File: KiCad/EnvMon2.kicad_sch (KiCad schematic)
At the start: 35 parts, among them J1 USB-C, J2 DC, J3 TEMP, M1 OLED1.5-RGB, SW1 SW_Push, SW2 SW_Push, SW3 SW_Push, U1 LMR16006+FB, U2 SCD41, U3 FT231XQ, U4 ESP32-PICO-MINI-02, U5 QR

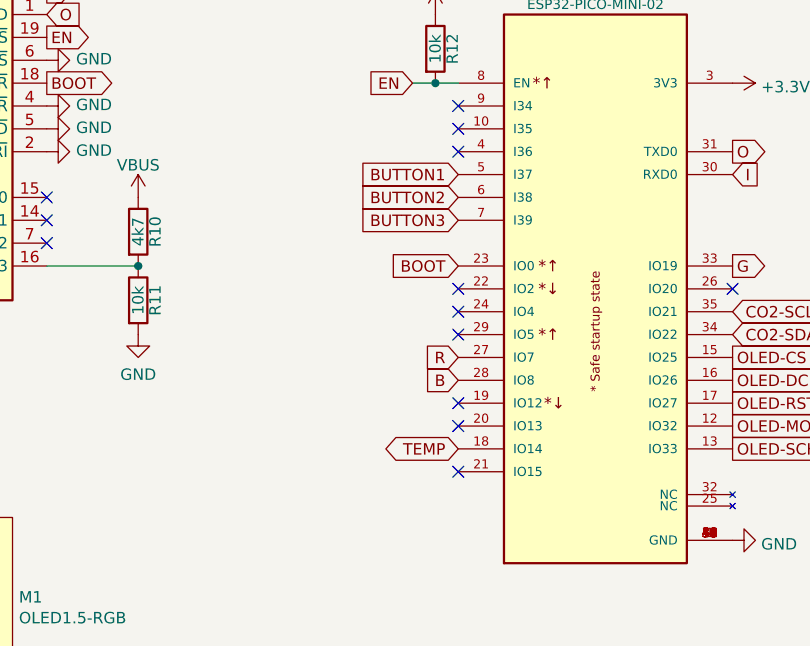
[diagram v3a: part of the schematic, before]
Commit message: Tidy GPIO usage for buttons
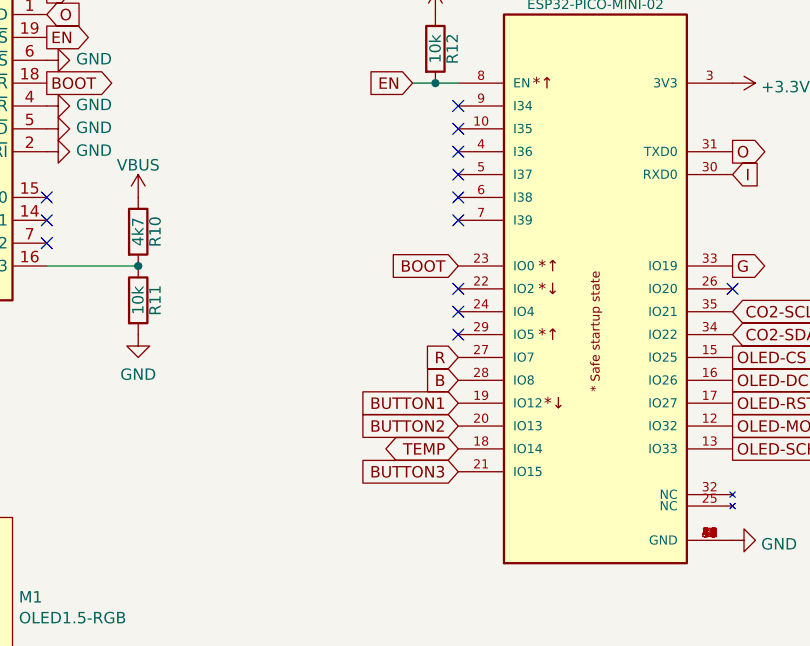
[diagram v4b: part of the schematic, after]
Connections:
- net BUTTON1: now also U4.19 (IO12); no longer U4.5 (I37)
- net BUTTON2: now also U4.20 (IO13); no longer U4.6 (I38)
- net BUTTON3: now also U4.21 (IO15); no longer U4.7 (I39)
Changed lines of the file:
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@@
   (no_connect (at 149.86 50.8))
   (no_connect (at 149.86 53.34))
-  (no_connect (at 195.58 76.2))
-  (no_connect (at 195.58 81.28))
+  (no_connect (at 195.58 50.8))
+  (no_connect (at 195.58 53.34))
   (no_connect (at 226.06 60.96))
   (no_connect (at 195.58 40.64))
@@
   (no_connect (at 195.58 60.96))
   (no_connect (at 195.58 66.04))
-  (no_connect (at 195.58 73.66))
+  (no_connect (at 195.58 48.26))
   (no_connect (at 195.58 63.5))
   (wire (pts (xy 55.88 33.02) (xy 58.42 33.02))
@@
     )
   )
-  (global_label "BUTTON2" (shape input) (at 195.58 50.8 180) (fields_autoplaced)
-    (effects (font (size 1.27 1.27)) (justify right))
-    (property "Intersheet References" "${INTERSHEET_REFS}" (id 0) (at 184.8496 50.7206 0)
+  (global_label "BUTTON2" (shape input) (at 195.58 76.2 180) (fields_autoplaced)
+    (effects (font (size 1.27 1.27)) (justify right))
+    (property "Intersheet References" "${INTERSHEET_REFS}" (id 0) (at 184.8496 76.1206 0)
       (effects (font (size 1.27 1.27)) (justify right) hide)
     )
@@
     )
   )
-  (global_label "BUTTON3" (shape input) (at 195.58 53.34 180) (fields_autoplaced)
-    (effects (font (size 1.27 1.27)) (justify right))
-    (property "Intersheet References" "${INTERSHEET_REFS}" (id 0) (at 184.8496 53.2606 0)
+  (global_label "BUTTON3" (shape input) (at 195.58 81.28 180) (fields_autoplaced)
+    (effects (font (size 1.27 1.27)) (justify right))
+    (property "Intersheet References" "${INTERSHEET_REFS}" (id 0) (at 184.8496 81.2006 0)
       (effects (font (size 1.27 1.27)) (justify right) hide)
     )
@@
     )
   )
-  (global_label "BUTTON1" (shape input) (at 195.58 48.26 180) (fields_autoplaced)
-    (effects (font (size 1.27 1.27)) (justify right))
-    (property "Intersheet References" "${INTERSHEET_REFS}" (id 0) (at 184.8496 48.1806 0)
-      (effects (font (size 1.27 1.27)) (justify right) hide)
-    )
+  (global_label "BUTTON1" (shape input) (at 195.58 73.66 180) (fields_autoplaced)
+    (effects (font (size 1.27 1.27)) (justify right))
+    (property "Intersheet References" "${INTERSHEET_REFS}" (id 0) (at 184.8496 73.5806 0)
+      (effects (font (size 1.27 1.27)) (justify right) hide)
+    )

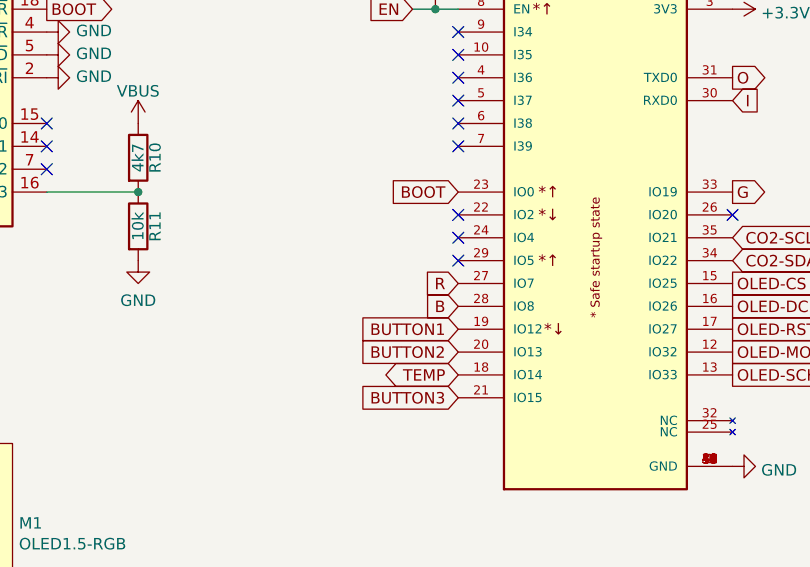
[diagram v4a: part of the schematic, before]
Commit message: Change GPIo for button1
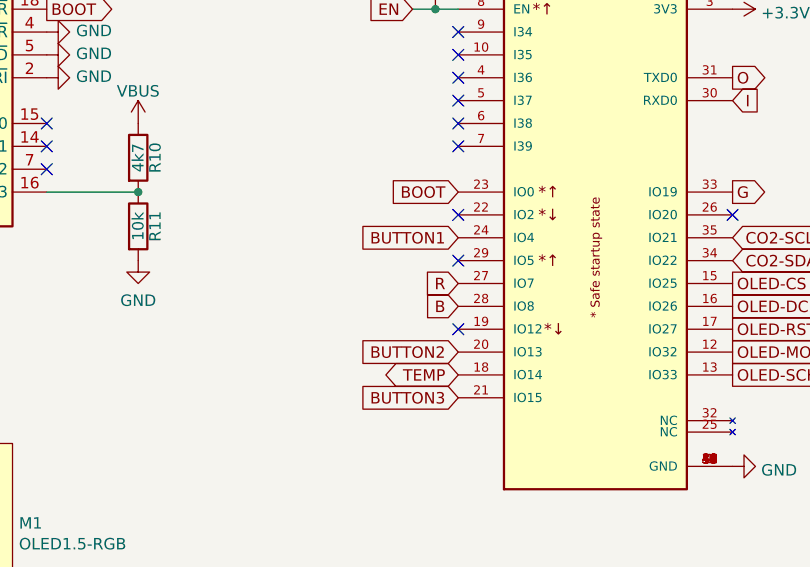
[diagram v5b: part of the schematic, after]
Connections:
- net BUTTON1: now also U4.24 (IO4); no longer U4.19 (IO12)
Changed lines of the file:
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@@
   (no_connect (at 195.58 66.04))
   (no_connect (at 195.58 48.26))
-  (no_connect (at 195.58 63.5))
+  (no_connect (at 195.58 73.66))
   (wire (pts (xy 55.88 33.02) (xy 58.42 33.02))
     (stroke (width 0) (type default) (color 0 0 0 0))
@@
     )
   )
-  (global_label "BUTTON1" (shape input) (at 195.58 73.66 180) (fields_autoplaced)
-    (effects (font (size 1.27 1.27)) (justify right))
-    (property "Intersheet References" "${INTERSHEET_REFS}" (id 0) (at 184.8496 73.5806 0)
-      (effects (font (size 1.27 1.27)) (justify right) hide)
-    )
+  (global_label "BUTTON1" (shape input) (at 195.58 63.5 180) (fields_autoplaced)
+    (effects (font (size 1.27 1.27)) (justify right))
+    (property "Intersheet References" "${INTERSHEET_REFS}" (id 0) (at 184.8496 63.4206 0)
+      (effects (font (size 1.27 1.27)) (justify right) hide)
+    )

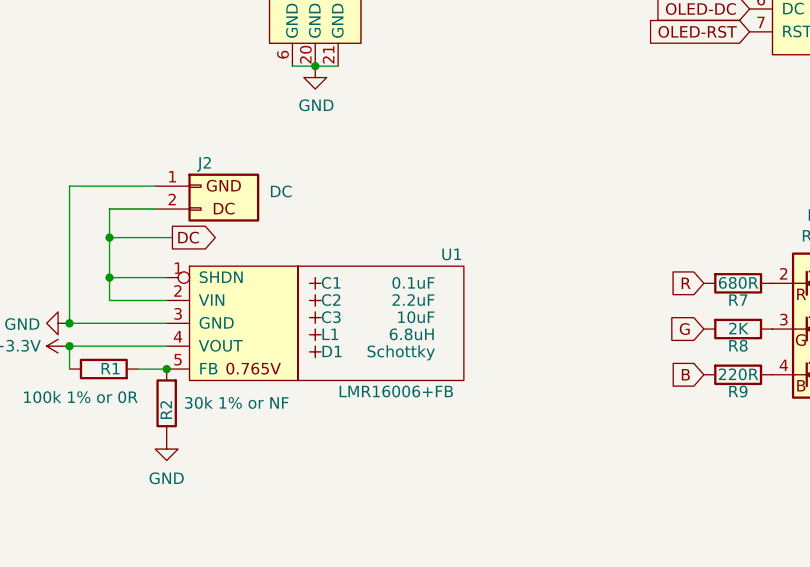
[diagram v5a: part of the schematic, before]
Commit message: Updated regulator
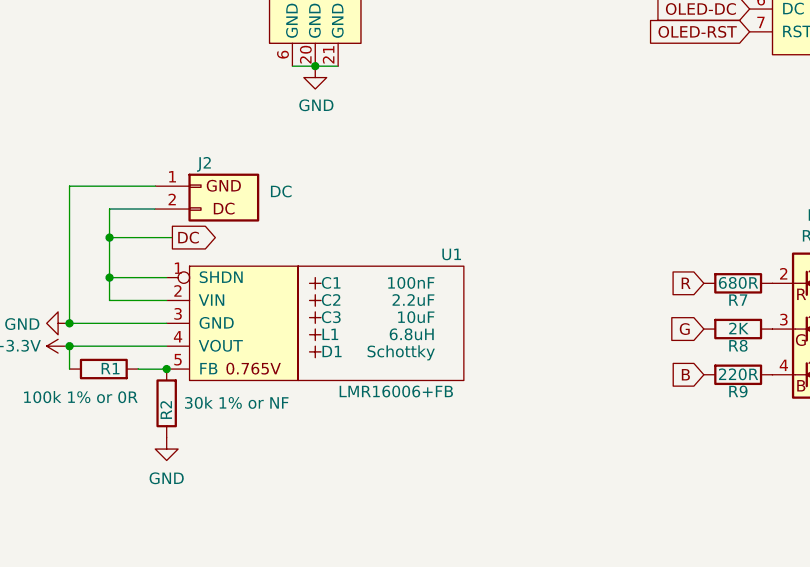
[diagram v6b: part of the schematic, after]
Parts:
- C1: value 0.1uF -> 100nF; footprint RevK:Hidden -> RevK:C_0603_
- C2, C3: footprint RevK:Hidden -> RevK:C_0805_
- D1: footprint RevK:Hidden -> RevK:D_1206_
- L1: footprint RevK:Hidden -> RevK:L_4x4_
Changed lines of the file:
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@@
       (effects (font (size 1.27 1.27)) (justify left))
     )
-    (property "Value" "0.1uF" (id 1) (at 79.375 132.08 0)
-      (effects (font (size 1.27 1.27)) (justify right))
-    )
-    (property "Footprint" "RevK:Hidden" (id 2) (at 66.04 132.08 0)
+    (property "Value" "100nF" (id 1) (at 79.375 132.08 0)
+      (effects (font (size 1.27 1.27)) (justify right))
+    )
+    (property "Footprint" "RevK:C_0603_" (id 2) (at 66.04 132.08 0)
       (effects (font (size 1.27 1.27)) hide)
     )
@@
       (effects (font (size 1.27 1.27)) (justify right))
     )
-    (property "Footprint" "RevK:Hidden" (id 2) (at 66.04 133.985 0)
+    (property "Footprint" "RevK:C_0805_" (id 2) (at 66.04 133.985 0)
       (effects (font (size 1.27 1.27)) hide)
     )
@@
       (effects (font (size 1.27 1.27)) (justify right))
     )
-    (property "Footprint" "RevK:Hidden" (id 2) (at 66.04 135.89 0)
+    (property "Footprint" "RevK:C_0805_" (id 2) (at 66.04 135.89 0)
       (effects (font (size 1.27 1.27)) hide)
     )
@@
       (effects (font (size 1.27 1.27)) (justify right))
     )
-    (property "Footprint" "RevK:Hidden" (id 2) (at 66.04 137.795 0)
+    (property "Footprint" "RevK:L_4x4_" (id 2) (at 66.04 137.795 0)
       (effects (font (size 1.27 1.27)) hide)
     )
@@
       (effects (font (size 1.27 1.27)) (justify right))
     )
-    (property "Footprint" "RevK:Hidden" (id 2) (at 66.04 139.7 0)
+    (property "Footprint" "RevK:D_1206_" (id 2) (at 66.04 139.7 0)
       (effects (font (size 1.27 1.27)) hide)
     )
@@
     )
     (path "/00000000-0000-0000-0000-0000610f9b88"
-      (reference "C1") (unit 1) (value "0.1uF") (footprint "RevK:Hidden")
+      (reference "C1") (unit 1) (value "100nF") (footprint "RevK:C_0603_")
     )
     (path "/00000000-0000-0000-0000-0000610fd0ef"
-      (reference "C2") (unit 1) (value "2.2uF") (footprint "RevK:Hidden")
+      (reference "C2") (unit 1) (value "2.2uF") (footprint "RevK:C_0805_")
     )
     (path "/00000000-0000-0000-0000-0000610fd80e"
-      (reference "C3") (unit 1) (value "10uF") (footprint "RevK:Hidden")
+      (reference "C3") (unit 1) (value "10uF") (footprint "RevK:C_0805_")
     )
     (path "/89b4a707-c1ed-4546-9194-77a5268f4f37"
@@
     )
     (path "/00000000-0000-0000-0000-0000610fe5d2"
-      (reference "D1") (unit 1) (value "Schottky") (footprint "RevK:Hidden")
+      (reference "D1") (unit 1) (value "Schottky") (footprint "RevK:D_1206_")
     )
     (path "/bbc62690-b8fb-438a-8ee0-c77d65956f89"
@@
     )
     (path "/00000000-0000-0000-0000-0000610fe01a"
-      (reference "L1") (unit 1) (value "6.8uH") (footprint "RevK:Hidden")
+      (reference "L1") (unit 1) (value "6.8uH") (footprint "RevK:L_4x4_")
     )
     (path "/9e3612ff-8ec7-4d75-b7a1-c8aca77044d4"

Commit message: Some PCB rework in progress
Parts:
- added J4: Shelly, RevK:Shelly, symbol RevK:Shelly
- added U6: VEML3235SL, RevK:VEML3235SL, symbol RevK:VEML3235SL
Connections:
- net +3V3: now also J4.3 (3V3), U6.1 (VDD)
- net BOOT: now also J4.4 (Rx)
- net G: now also U4.29 (IO5); no longer U4.33 (IO19)
- net GND: now also J4.5 (Tx), U6.2 (GND)
- net I: now also J4.2 (0)
- net O: now also J4.1 (GND)
- net LIGHT-SCL: now reaches U4.26 (IO20)
- net LIGHT-SCL: now also U6.4 (SCL)
- new net LIGHT-SDA: U4.33 (IO19), U6.3 (SDA)
- no-connect marks 13 -> 11

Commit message: Revised PCB for light sensor
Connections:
- net G: now also U4.33 (IO19); no longer U4.29 (IO5)
- net CO2-SCL renamed SCL
- net SCL: now also U6.4 (SCL)
- net CO2-SDA renamed SDA
- net SDA: now also U6.3 (SDA)
- net LIGHT-SCL: no longer names the net of U4.26 (IO20)
- net LIGHT-SCL: no longer U6.4 (SCL)
- removed net LIGHT-SDA: U4.33 (IO19), U6.3 (SDA)
- no-connect marks 11 -> 13
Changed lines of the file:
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@@
   )
   (no_connect (at 149.86 55.88))
+  (no_connect (at 195.58 66.04))
+  (no_connect (at 226.06 60.96))
   (no_connect (at 149.86 50.8))
   (no_connect (at 149.86 53.34))
@@
     )
   )
-  (global_label "LIGHT-SCL" (shape bidirectional) (at 226.06 60.96 0) (fields_autoplaced)
-    (effects (font (size 1.27 1.27)) (justify left))
-    (property "Intersheet References" "${INTERSHEET_REFS}" (id 0) (at 238.6652 61.0394 0)
-      (effects (font (size 1.27 1.27)) (justify left) hide)
-    )
-  )
   (global_label "TEMP" (shape bidirectional) (at 198.12 134.62 180) (fields_autoplaced)
     (effects (font (size 1.27 1.27)) (justify right))
@@
     )
   )
-  (global_label "CO2-SCL" (shape input) (at 226.06 63.5 0) (fields_autoplaced)
-    (effects (font (size 1.27 1.27)) (justify left))
-    (property "Intersheet References" "${INTERSHEET_REFS}" (id 0) (at 274.955 184.785 0)
-      (effects (font (size 1.27 1.27)) hide)
+  (global_label "SCL" (shape output) (at 226.06 63.5 0) (fields_autoplaced)
+    (effects (font (size 1.27 1.27)) (justify left))
+    (property "Intersheet References" "${INTERSHEET_REFS}" (id 0) (at 231.8918 63.4206 0)
+      (effects (font (size 1.27 1.27)) (justify left) hide)
     )
   )
@@
     )
   )
-  (global_label "LIGHT-SDA" (shape bidirectional) (at 157.48 138.43 180) (fields_autoplaced)
-    (effects (font (size 1.27 1.27)) (justify right))
-    (property "Intersheet References" "${INTERSHEET_REFS}" (id 0) (at 144.8144 138.3506 0)
+  (global_label "SDA" (shape bidirectional) (at 157.48 138.43 180) (fields_autoplaced)
+    (effects (font (size 1.27 1.27)) (justify right))
+    (property "Intersheet References" "${INTERSHEET_REFS}" (id 0) (at 151.5877 138.3506 0)
       (effects (font (size 1.27 1.27)) (justify right) hide)
     )
@@
     )
   )
-  (global_label "CO2-SCL" (shape input) (at 58.42 93.98 180) (fields_autoplaced)
-    (effects (font (size 1.27 1.27)) (justify right))
-    (property "Intersheet References" "${INTERSHEET_REFS}" (id 0) (at 9.525 -27.305 0)
-      (effects (font (size 1.27 1.27)) hide)
-    )
-  )
-  (global_label "LIGHT-SCL" (shape bidirectional) (at 157.48 140.97 180) (fields_autoplaced)
-    (effects (font (size 1.27 1.27)) (justify right))
-    (property "Intersheet References" "${INTERSHEET_REFS}" (id 0) (at 144.8748 140.8906 0)
+  (global_label "SCL" (shape input) (at 58.42 93.98 180) (fields_autoplaced)
+    (effects (font (size 1.27 1.27)) (justify right))
+    (property "Intersheet References" "${INTERSHEET_REFS}" (id 0) (at 52.5882 93.9006 0)
+      (effects (font (size 1.27 1.27)) (justify right) hide)
+    )
+  )
+  (global_label "SCL" (shape input) (at 157.48 140.97 180) (fields_autoplaced)
+    (effects (font (size 1.27 1.27)) (justify right))
+    (property "Intersheet References" "${INTERSHEET_REFS}" (id 0) (at 151.6482 140.8906 0)
       (effects (font (size 1.27 1.27)) (justify right) hide)
     )
@@
     )
   )
-  (global_label "G" (shape output) (at 195.58 66.04 180) (fields_autoplaced)
-    (effects (font (size 1.27 1.27)) (justify right))
-    (property "Intersheet References" "${INTERSHEET_REFS}" (id 0) (at 191.9858 66.1194 0)
-      (effects (font (size 1.27 1.27)) (justify right) hide)
+  (global_label "G" (shape output) (at 226.06 58.42 0) (fields_autoplaced)
+    (effects (font (size 1.27 1.27)) (justify left))
+    (property "Intersheet References" "${INTERSHEET_REFS}" (id 0) (at 229.6542 58.3406 0)
+      (effects (font (size 1.27 1.27)) (justify left) hide)
     )
   )
@@
     )
   )
-  (global_label "CO2-SDA" (shape bidirectional) (at 226.06 66.04 0) (fields_autoplaced)
-    (effects (font (size 1.27 1.27)) (justify left))
-    (property "Intersheet References" "${INTERSHEET_REFS}" (id 0) (at 237.3347 65.9606 0)
+  (global_label "SDA" (shape bidirectional) (at 226.06 66.04 0) (fields_autoplaced)
+    (effects (font (size 1.27 1.27)) (justify left))
+    (property "Intersheet References" "${INTERSHEET_REFS}" (id 0) (at 231.9523 65.9606 0)
       (effects (font (size 1.27 1.27)) (justify left) hide)
     )
@@
     )
   )
-  (global_label "LIGHT-SDA" (shape bidirectional) (at 226.06 58.42 0) (fields_autoplaced)
-    (effects (font (size 1.27 1.27)) (justify left))
-    (property "Intersheet References" "${INTERSHEET_REFS}" (id 0) (at 238.7256 58.4994 0)
-      (effects (font (size 1.27 1.27)) (justify left) hide)
-    )
-  )
-  (global_label "CO2-SDA" (shape bidirectional) (at 58.42 91.44 180) (fields_autoplaced)
-    (effects (font (size 1.27 1.27)) (justify right))
-    (property "Intersheet References" "${INTERSHEET_REFS}" (id 0) (at 47.1453 91.3606 0)
-      (effects (font (size 1.27 1.27)) (justify right) hide)
-    )
+  (global_label "SDA" (shape bidirectional) (at 58.42 91.44 180) (fields_autoplaced)
+    (effects (font (size 1.27 1.27)) (justify right))
+    (property "Intersheet References" "${INTERSHEET_REFS}" (id 0) (at 52.5277 91.3606 0)
+      (effects (font (size 1.27 1.27)) (justify right) hide)
+    )
